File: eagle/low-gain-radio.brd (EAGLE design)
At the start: 99 x 100 mm, 125 parts, among them U1 MKW01Z128, U2 SKY65116, U3 W25Q80DV, U4 LP5907MFX-3.3, U5 NC7SZ05, U6 LP5907MFX-3.3, U7 LD39200, U8 MAAL-010704, U9 SKY13405-490LF, Y1 32MHz

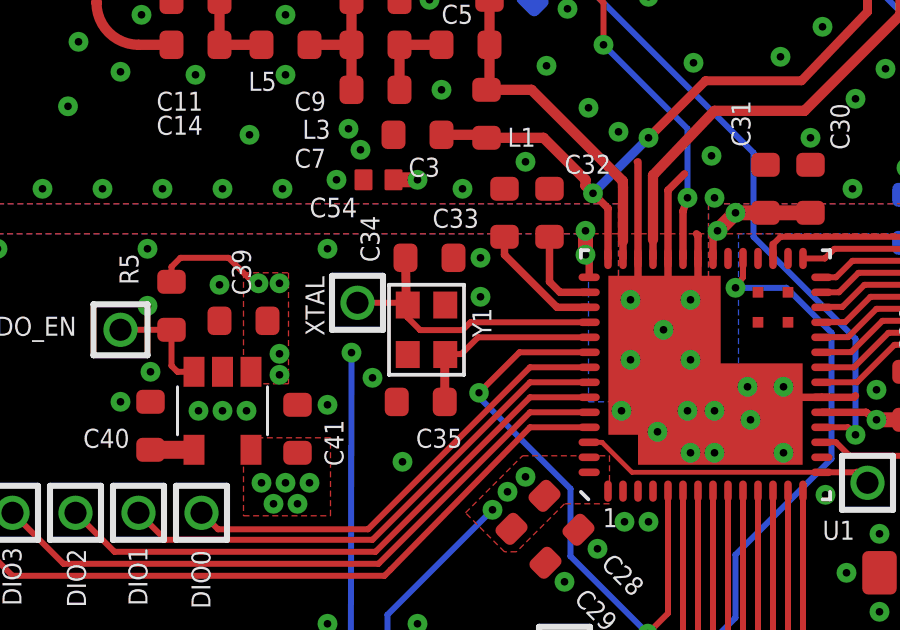
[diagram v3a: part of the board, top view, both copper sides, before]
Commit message: Changed crystal symbol to get gnd working on the layout
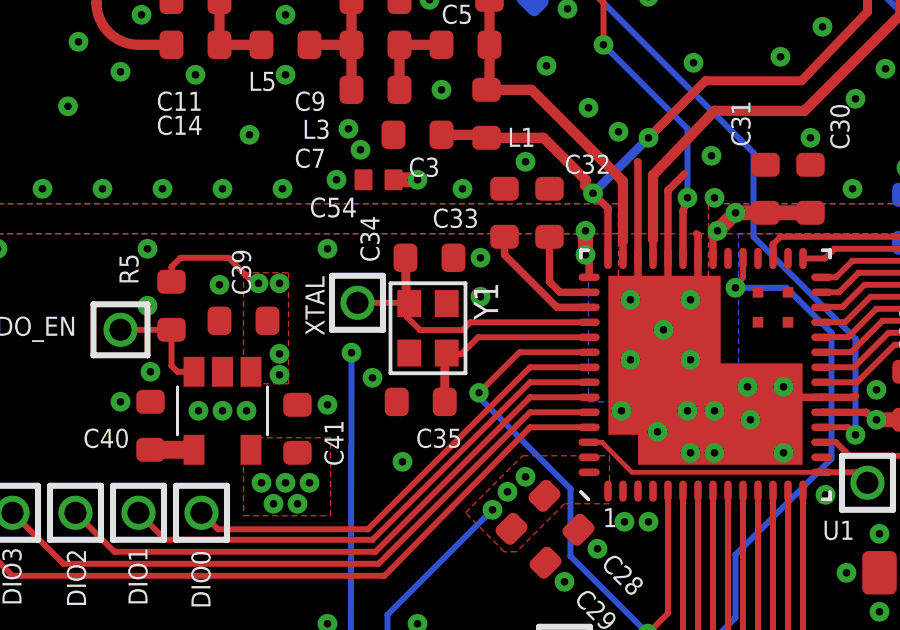
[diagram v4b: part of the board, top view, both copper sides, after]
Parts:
- Y1: value 32MHz -> (none); device microbuilder:CRYSTAL_2.5X2 -> low-gain-radio:CRYSTAL_2.5X2
- moved Y1 0.07 mm to (66.8, 59.9)
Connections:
- net GND: now also Y1.2, Y1.4
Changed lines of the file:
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@@
 <attribute name="VALUE" x="71" y="81.7" size="1.27" layer="27" font="vector" ratio="15" rot="R180"/>
-</element>
-<element name="Y1" library="microbuilder" package="CRYSTAL_2.5X2" value="32MHz" x="66.8" y="59.8" smashed="yes" rot="R270">
-<attribute name="MPN" value="FA20H 32.0000MF12Y-W3" x="66.8" y="59.8" size="1.778" layer="27" rot="R270" display="off"/>
-<attribute name="DIST" value="Digi-Key" x="66.8" y="59.8" size="1.778" layer="27" rot="R270" display="off"/>
-<attribute name="DPN" value="SER4044CT-ND" x="66.8" y="59.8" size="1.778" layer="27" rot="R270" display="off"/>
-<attribute name="MFN" value="EPSON" x="66.8" y="59.8" size="1.778" layer="27" rot="R270" display="off"/>
-<attribute name="NAME" x="68.328" y="60.532" size="0.635" layer="25" font="vector" ratio="20" rot="R270"/>
-<attribute name="VALUE" x="64.891" y="61.205" size="0.4064" layer="27" ratio="10" rot="R270"/>
 </element>
 <element name="C23" library="rcl_custom" package=".0402-B-NOSILK" value="1nF" x="75.2" y="83.7" smashed="yes">
@@
 <attribute name="MFG" value="Yageo" x="92.1" y="2.05" size="1.778" layer="27" rot="R90" display="off"/>
 </element>
+<element name="Y1" library="low-gain-radio" package="CRYSTAL_2.5X2" value="" x="66.85" y="59.85" rot="R270"/>
 </elements>
 <signals>
@@
 <contactref element="LED9" pad="K"/>
 <contactref element="LED10" pad="K"/>
+<contactref element="Y1" pad="2"/>
+<contactref element="Y1" pad="4"/>
 </signal>
 <signal name="SWD_DIO">
@@
 <contactref element="U1" pad="46"/>
 <contactref element="C34" pad="2"/>
-<contactref element="Y1" pad="1"/>
-<wire x1="66.175" y1="60.625" x2="66.1279125" y2="60.642253125" width="0.3" layer="1"/>
-<wire x1="66.1279125" y1="60.642253125" x2="66.1" y2="62.2" width="0.3" layer="1"/>
+<wire x1="66.1279125" y1="60.642253125" x2="66.12686875" y2="60.70048125" width="0.3" layer="1"/>
+<wire x1="66.12686875" y1="60.70048125" x2="66.1" y2="62.2" width="0.3" layer="1"/>
 <wire x1="68.002228125" y1="59.789946875" x2="66.588015625" y2="59.789946875" width="0.2" layer="1"/>
 <wire x1="66.588015625" y1="59.789946875" x2="66.16375" y2="60.2142125" width="0.2" layer="1"/>
 <wire x1="66.16375" y1="60.2142125" x2="66.16375" y2="60.6214125" width="0.2" layer="1"/>
-<wire x1="66.16375" y1="60.6214125" x2="66.175" y2="60.625" width="0.2" layer="1"/>
 <wire x1="72.2222" y1="60.05" x2="68.26228125" y2="60.05" width="0.2" layer="1"/>
 <wire x1="68.26228125" y1="60.05" x2="68.002228125" y2="59.789946875" width="0.2" layer="1"/>
 <contactref element="XTAL" pad="1"/>
 <wire x1="64.5" y1="60.7" x2="66.1" y2="60.7" width="0.2" layer="1"/>
-<wire x1="66.1" y1="60.7" x2="66.175" y2="60.625" width="0.2" layer="1"/>
+<contactref element="Y1" pad="1"/>
+<wire x1="66.12686875" y1="60.7" x2="66.225" y2="60.7" width="0.4064" layer="1"/>
+<wire x1="66.225" y1="60.7" x2="66.225" y2="60.675" width="0.4064" layer="1"/>
+<wire x1="66.1" y1="60.7" x2="66.12686875" y2="60.7" width="0.4064" layer="1"/>
+<wire x1="66.12686875" y1="60.7" x2="66.12686875" y2="60.70048125" width="0.4064" layer="1"/>
+<wire x1="66.1279125" y1="60.642253125" x2="66.16375" y2="60.6214125" width="0" layer="19" extent="1-1"/>
 </signal>
 <signal name="N$8">
 <contactref element="U1" pad="47"/>
 <contactref element="C35" pad="2"/>
-<contactref element="Y1" pad="3"/>
-<wire x1="67.425" y1="58.975" x2="67.4079125" y2="58.99225625" width="0.3" layer="1"/>
 <wire x1="67.4079125" y1="58.99225625" x2="67.4079125" y2="57.39725625" width="0.3" layer="1"/>
-<wire x1="67.96" y1="58.99" x2="67.395165625" y2="58.99" width="0.2" layer="1"/>
-<wire x1="67.395165625" y1="58.99" x2="67.425" y2="58.975" width="0.2" layer="1"/>
+<wire x1="67.96" y1="58.99" x2="67.45" y2="58.99" width="0.2" layer="1"/>
+<wire x1="67.45" y1="58.99" x2="67.395165625" y2="58.99" width="0.2" layer="1"/>
 <wire x1="72.2222" y1="59.55" x2="68.52" y2="59.55" width="0.2" layer="1"/>
 <wire x1="68.52" y1="59.55" x2="67.96" y2="58.99" width="0.2" layer="1"/>
+<contactref element="Y1" pad="3"/>
+<wire x1="67.475" y1="59.025" x2="67.45" y2="58.975" width="0.4064" layer="1"/>
+<wire x1="67.45" y1="58.975" x2="67.45" y2="58.99" width="0.4064" layer="1"/>
+<wire x1="67.395165625" y1="58.99" x2="67.4079125" y2="58.99" width="0.4064" layer="1"/>
+<wire x1="67.4079125" y1="58.99" x2="67.4079125" y2="58.99225625" width="0.4064" layer="1"/>
 </signal>
 <signal name="UART0_RX">

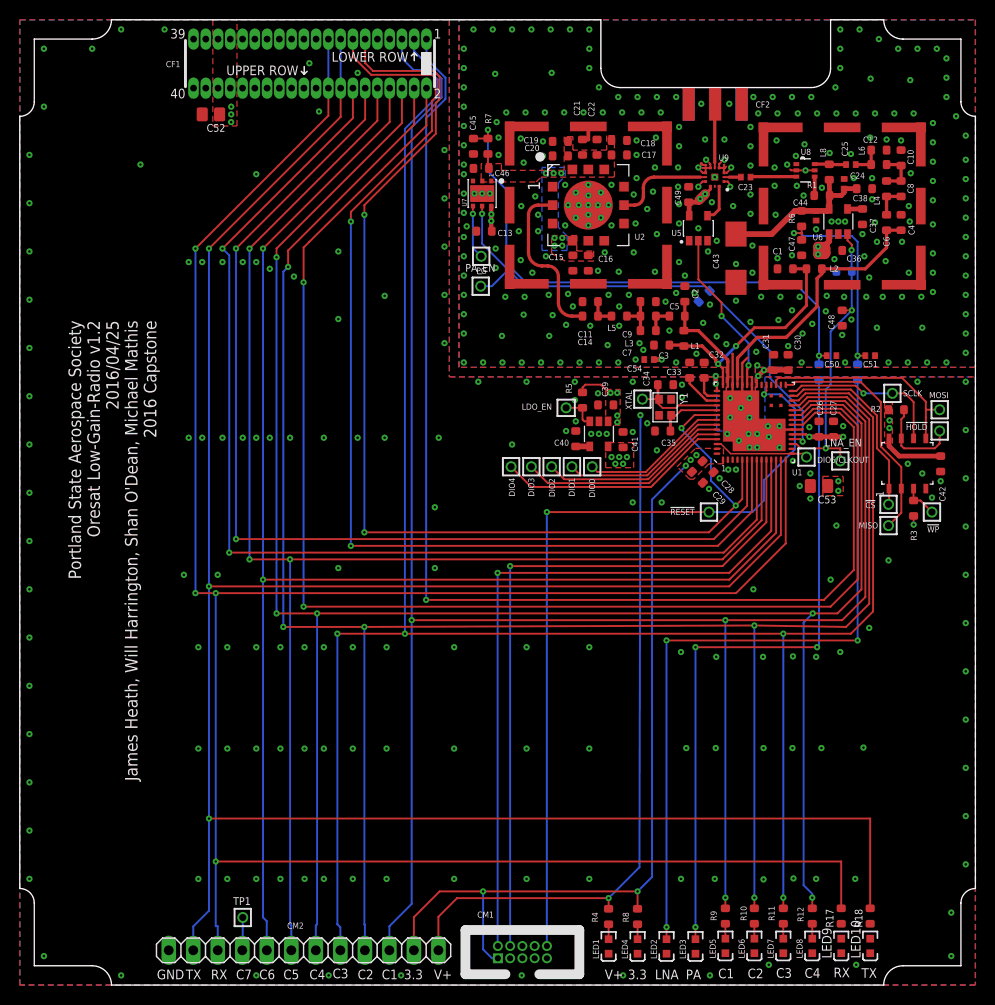
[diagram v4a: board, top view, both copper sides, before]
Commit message: Updated firmware
New: CMSIS submodule

Updated drivers
Added interrupt functionality
printf on uart0 with interrupts
doxygen template added
new project organization and test project
updated organization for firmware
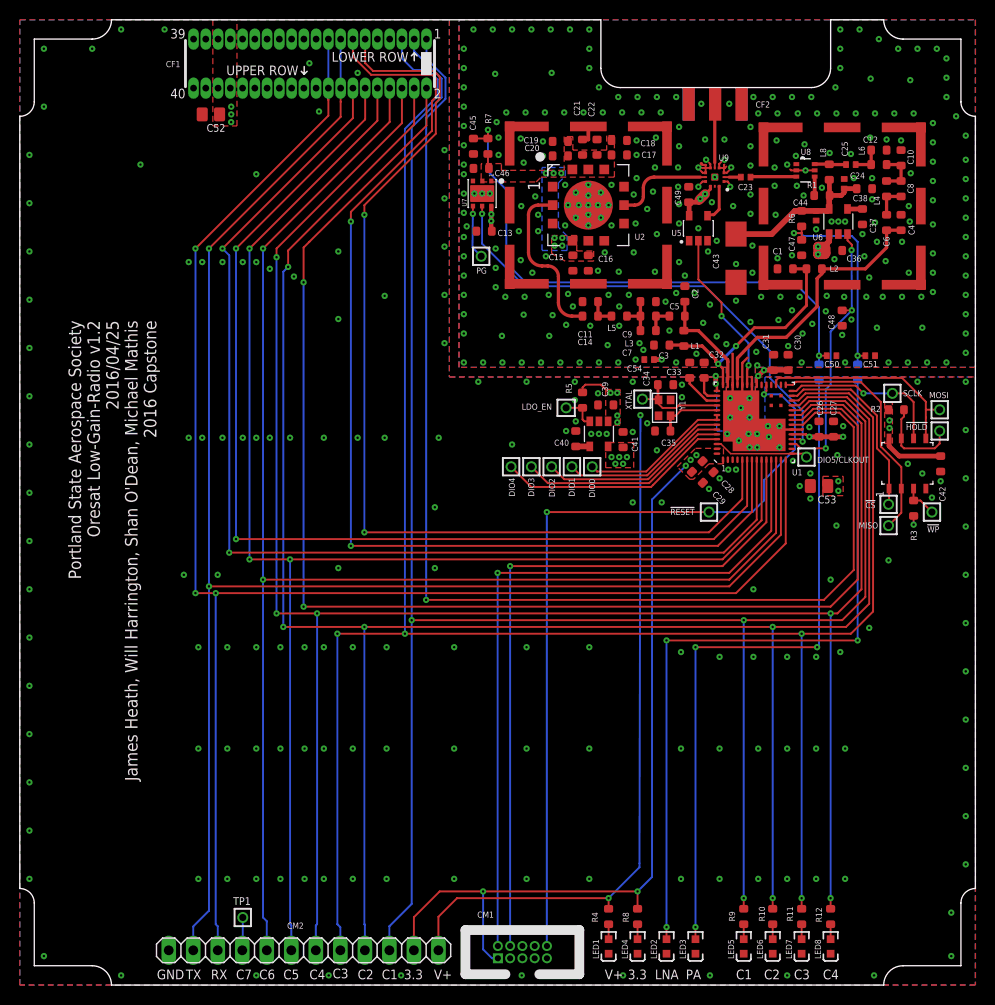
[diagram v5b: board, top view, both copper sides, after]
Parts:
- removed LED10, LED9: DNP/GRN, psas_c3_team05:LED-0603
- removed LNA_EN, PA_EN: TEST-POINT, Tova:2MM-TEST-POINT
- removed R15, R16: 10k, rcl_custom:.0603-B-NOSILK@1
- removed R17, R18: DNP/1k, rcl_custom:.0603-B-NOSILK@1
- Y1: value (none) -> 32MHz; device low-gain-radio:CRYSTAL_2.5X2 -> microbuilder:CRYSTAL_2.5X2
- moved LED5 1.90 mm to (75.0, 4.00)
- moved LED6 1.90 mm to (78.0, 4.00)
- moved LED7 1.90 mm to (81.0, 4.00)
- moved LED8 1.90 mm to (84.0, 4.00)
- moved R10 1.90 mm to (78.0, 7.10)
- moved R11 1.90 mm to (81.0, 7.10)
- moved R12 1.90 mm to (84.0, 7.10)
- moved R9 1.90 mm to (75.0, 7.10)
- moved Y1 0.07 mm to (66.8, 59.8)
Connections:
- removed net N$11: DIO0.1, U1.49
- removed net N$6: LED9.A, R17.1
- removed net N$9: LED10.A, R18.1
- new net DIO0: DIO0.1, U1.48, U1.49
- net GND: no longer LED10.K, LED9.K, Y1.2, Y1.4
- net LNA_EN: no longer LNA_EN.1, R16.1
- net PA_EN: no longer PA_EN.1, R15.1
- net PTE16: no longer U1.48
- net RF_GND: no longer R15.2, R16.2
- net UART0_RX: no longer R17.2
- net UART0_TX: no longer R18.2
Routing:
- net UART0_TX: track 247.8 -> 170.0 mm, vias 3 -> 2
- net UART0_RX: track 241.9 -> 172.1 mm, vias 4 -> 3
- net DIO0: track 0.00 -> 15.8 mm
- net N$11: track 15.4 -> 0.00 mm
- net PTE16: track 120.5 -> 105.9 mm, vias 4 -> 2
- net PA_EN: track 54.0 -> 50.3 mm
- net LNA_EN: track 31.1 -> 28.2 mm
- net PTC4: track 213.4 -> 212.6 mm
- net RF_GND: vias 284 -> 285
- net GND: vias 180 -> 181

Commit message: Added new RF switch
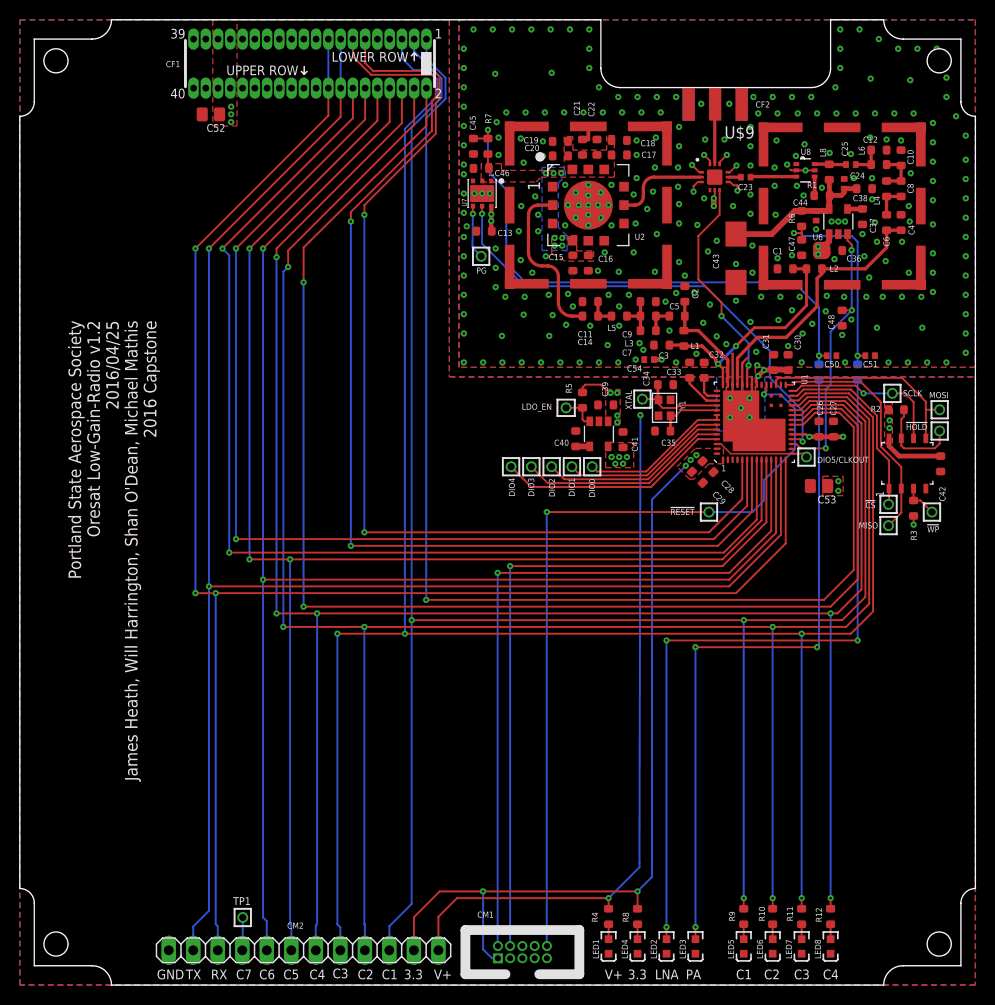
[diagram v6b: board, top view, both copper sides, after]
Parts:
- removed C49: 100nF, rcl_custom:.0603-B-NOSILK
- removed U5: NC7SZ05, psas_c3_team05:NC7SZ05
- removed U9: SKY13405-490LF, psas_c3_team05:SKY13405-490LF
- added U$9: PE42723, low-gain-radio:PE42723
- turned U1 to 90 degrees
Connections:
- removed net !RXTX: U5.4, U9.12
- new net NC: U$9.4
- net LNA_IN: now also U$9.8; no longer U9.2
- net N$30: now also U$9.11; no longer U9.5
- net PA_IN: now also U$9.2; no longer U9.8
- net RF_GND: now also U$9.1, U$9.10, U$9.12, U$9.3, U$9.7, U$9.9; no longer C49.1, U5.3, U9.1, U9.11, U9.3, U9.4, U9.6, U9.7, U9.9, U9.CENTER
- net RXTX: now also U$9.6; no longer U5.2
- net V+: now also U$9.5; no longer C49.2, U5.5, U9.10
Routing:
- net RXTX: track 17.1 -> 23.3 mm
- net GND: track 4.96 -> 0.00 mm, vias 181 -> 0
- net !RXTX: track 3.87 -> 0.00 mm
- net V+: track 91.5 -> 88.4 mm
- net 3.3V: track 102.4 -> 100.8 mm, vias 21 -> 19
- net RF_GND: vias 285 -> 284

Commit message: LGR SCHEMATIC AND BOARD REVISIONS
1. Added 0 ohms on VOUT of all LDOs
2. Created reflectometer circuit
3. Got rid of GPIO bus to 40 pin connector
4. Started layout for the 0ohm resistors and reflectometer but it got awfully messy and there are major changes that are going to be made to the board outline and antenna connector so I left them undone
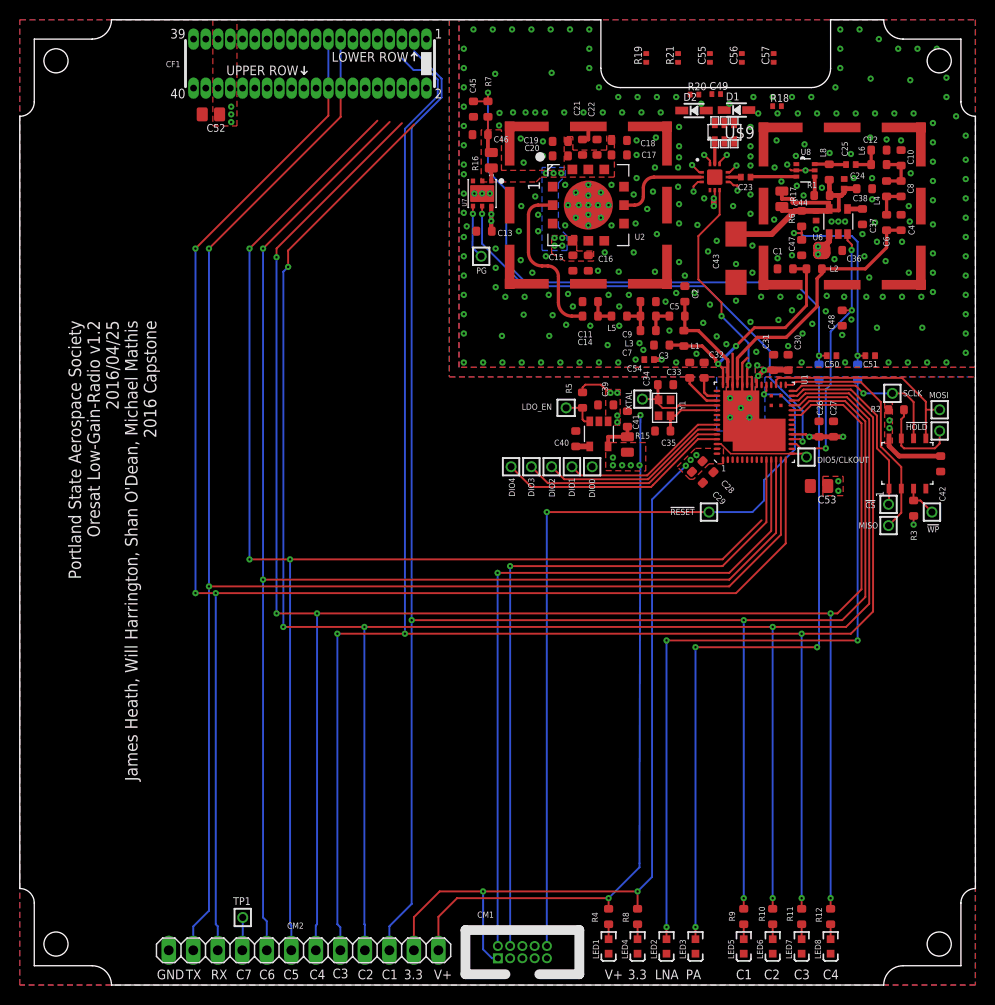
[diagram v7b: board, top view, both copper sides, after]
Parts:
- removed CF2: CON-MCX-F-LINX-CONMCX003.062, oresat-eagle:CON-MCX-LINX-CONMCX003.062
- added C49, C55, C56, C57: 47nF, low-gain-radio:.0402-C-NOSILK
- added D1, D2: 1N5711WS, microbuilder:SOD-323
- added R15, R16, R17: 0, low-gain-radio:.0805-C-NOSILK$1
- added R18, R19: 51, low-gain-radio:.0402-C-NOSILK$1
- added R20, R21: 20k, low-gain-radio:.0402-C-NOSILK$1
- added U$22: BDCN-20-13+, low-gain-radio:FV1206-1
- CM1: device psas_c3_team05:PINHEADER-2X5-0.05+POL+SILK -> low-gain-radio:PINHEADER-2X5-0.05+POL+SILK
- moved C45 3.85 mm to (47.0, 90.8)
- moved R7 3.85 mm to (48.5, 90.8)
- moved C46 3.50 mm to (47.7, 88.1)
- moved C41 2.20 mm to (63.0, 58.6)
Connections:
- removed net N$30: CF2.CENTER, U$9.11
- removed net NC: U$9.4
- removed net PTB17: CF1.P$2, U1.22
- removed net PTB2: CF1.P$1, U1.21
- removed net PTE16: CF1.P$11, U1.5
- removed net PTE17: CF1.P$12, U1.6
- removed net PTE18: CF1.P$13, U1.7
- removed net PTE19: CF1.P$14, U1.8
- new net DC_OUT: U$22.OUT
- new net FWD: D2.A, R19.2, U$22.FWD
- new net N$11: R17.1, U6.5
- new net N$24: C49.1, D1.C, R20.2
- new net N$28: C57.1, D2.C, R21.2
- new net N$6: C41.2, C53.1, R15.1, U4.5
- new net N$9: R16.1, U7.1
- new net REV: D1.A, R18.2, U$22.REV
- new net RFC: U$22.IN, U$9.11
- new net RF_RESET: U1.48, U1.5
- new net VFWD: C56.1, R21.1, U1.6
- new net VREV: C55.1, R20.1, U1.7
- net 3.3V: now also R15.2; no longer C41.2, C53.1, U4.5
- net DIO0: no longer U1.48
- net PTA4: no longer CF1.P$8
- net PTC1: no longer CF1.P$3
- net PTC2: no longer CF1.P$4
- net PTC3: no longer CF1.P$5
- net PTC4: no longer CF1.P$6
- net PTE30: no longer CF1.P$10
- net RF_GND: now also C49.2, C55.2, C56.2, C57.2, R18.1, R19.1, U$22.GND, U$22.GND2; no longer CF2.SHIELD1, CF2.SHIELD2, CF2.SHIELD3, CF2.SHIELD4
- net VBIAS: now also R17.2; no longer U6.5
- net VPA: now also R16.2; no longer U7.1
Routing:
- net PTB17: track 141.6 -> 0.00 mm, vias 2 -> 0
- net PTB2: track 127.7 -> 0.00 mm, vias 1 -> 0
- net PTE19: track 116.3 -> 0.00 mm, vias 2 -> 0
- net PTE18: track 111.8 -> 0.00 mm, vias 2 -> 0
- net PTE17: track 111.4 -> 0.00 mm, vias 2 -> 0
- net PTE16: track 105.9 -> 0.00 mm, vias 2 -> 0
- net DIO0: track 15.8 -> 0.00 mm
- net PTE30: track 155.9 -> 146.2 mm
- net N$11: track 0.00 -> 6.75 mm
- net N$30: track 6.23 -> 0.00 mm
- net N$6: track 0.00 -> 4.05 mm
- net V_PA_FILTERED: track 58.0 -> 61.8 mm
- net PTC2: track 214.3 -> 210.5 mm
- net PTC4: track 212.6 -> 209.0 mm
- net PTA4: track 157.6 -> 154.1 mm
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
